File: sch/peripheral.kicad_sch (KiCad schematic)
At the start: 0 parts

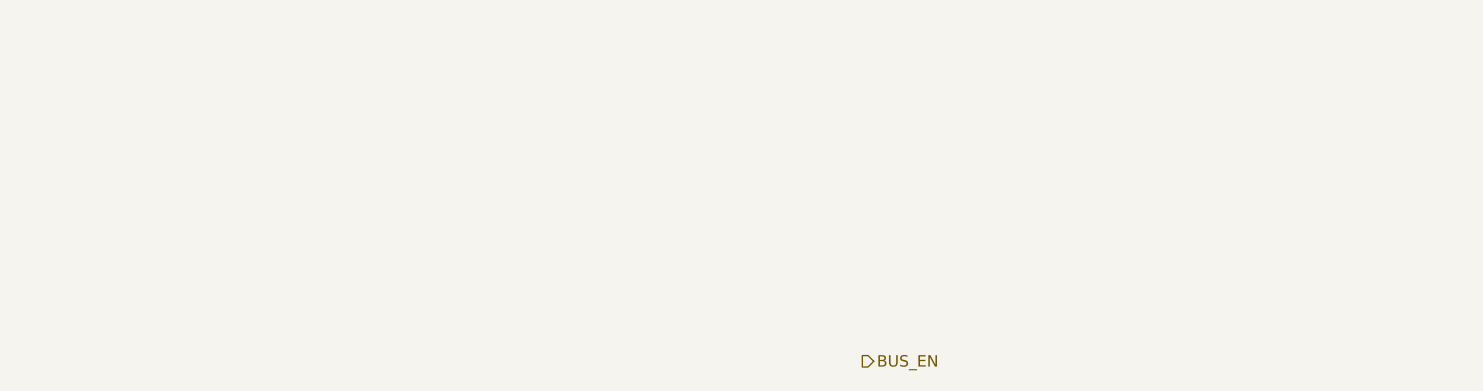
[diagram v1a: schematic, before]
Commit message: Board layout, addr bus
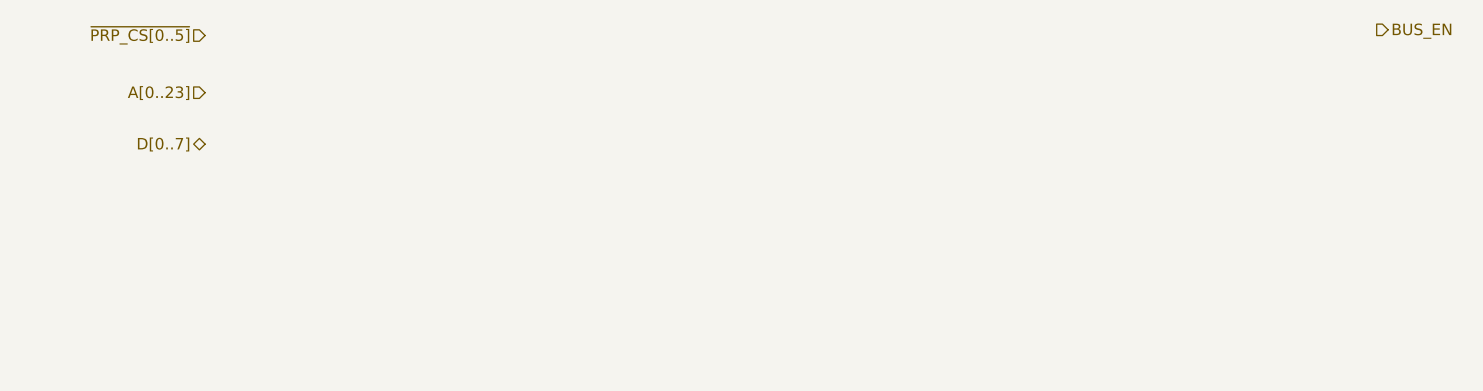
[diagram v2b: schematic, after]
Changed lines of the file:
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@@
 (kicad_sch (version 20211123) (generator eeschema)
   (paper "A4")
-  (hierarchical_label "BUS_EN" (shape output) (at 149.86 100.33 0)
+  (hierarchical_label "BUS_EN" (shape output) (at 207.01 63.5 0)
     (effects (font (size 1.27 1.27)) (justify left))
   )
+  (hierarchical_label "A[0..23]" (shape input) (at 76.835 70.485 180)
+    (effects (font (size 1.27 1.27)) (justify right))
+  )
+  (hierarchical_label "~{PRP_CS[0..5]}" (shape input) (at 76.835 64.135 180)
+    (effects (font (size 1.27 1.27)) (justify right))
+  )
+  (hierarchical_label "D[0..7]" (shape bidirectional) (at 76.835 76.2 180)
+    (effects (font (size 1.27 1.27)) (justify right))
+  )
 )

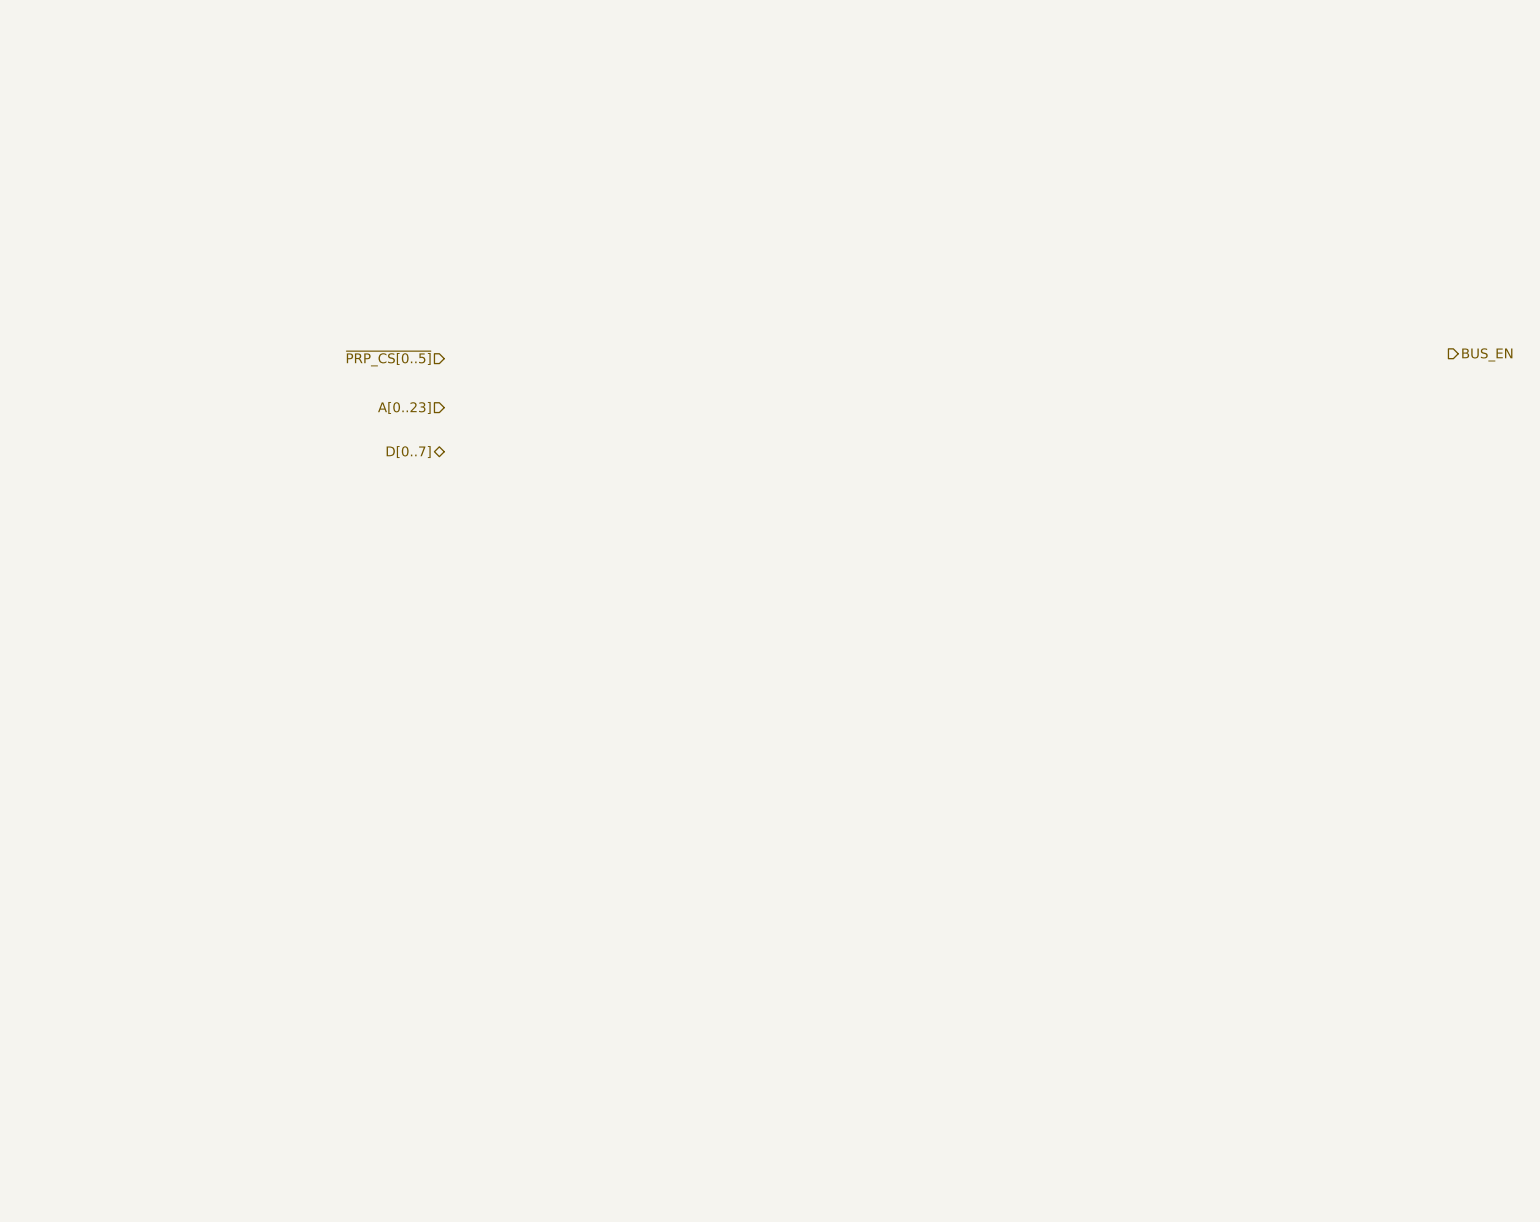
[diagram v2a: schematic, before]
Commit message: More routing, USB iface
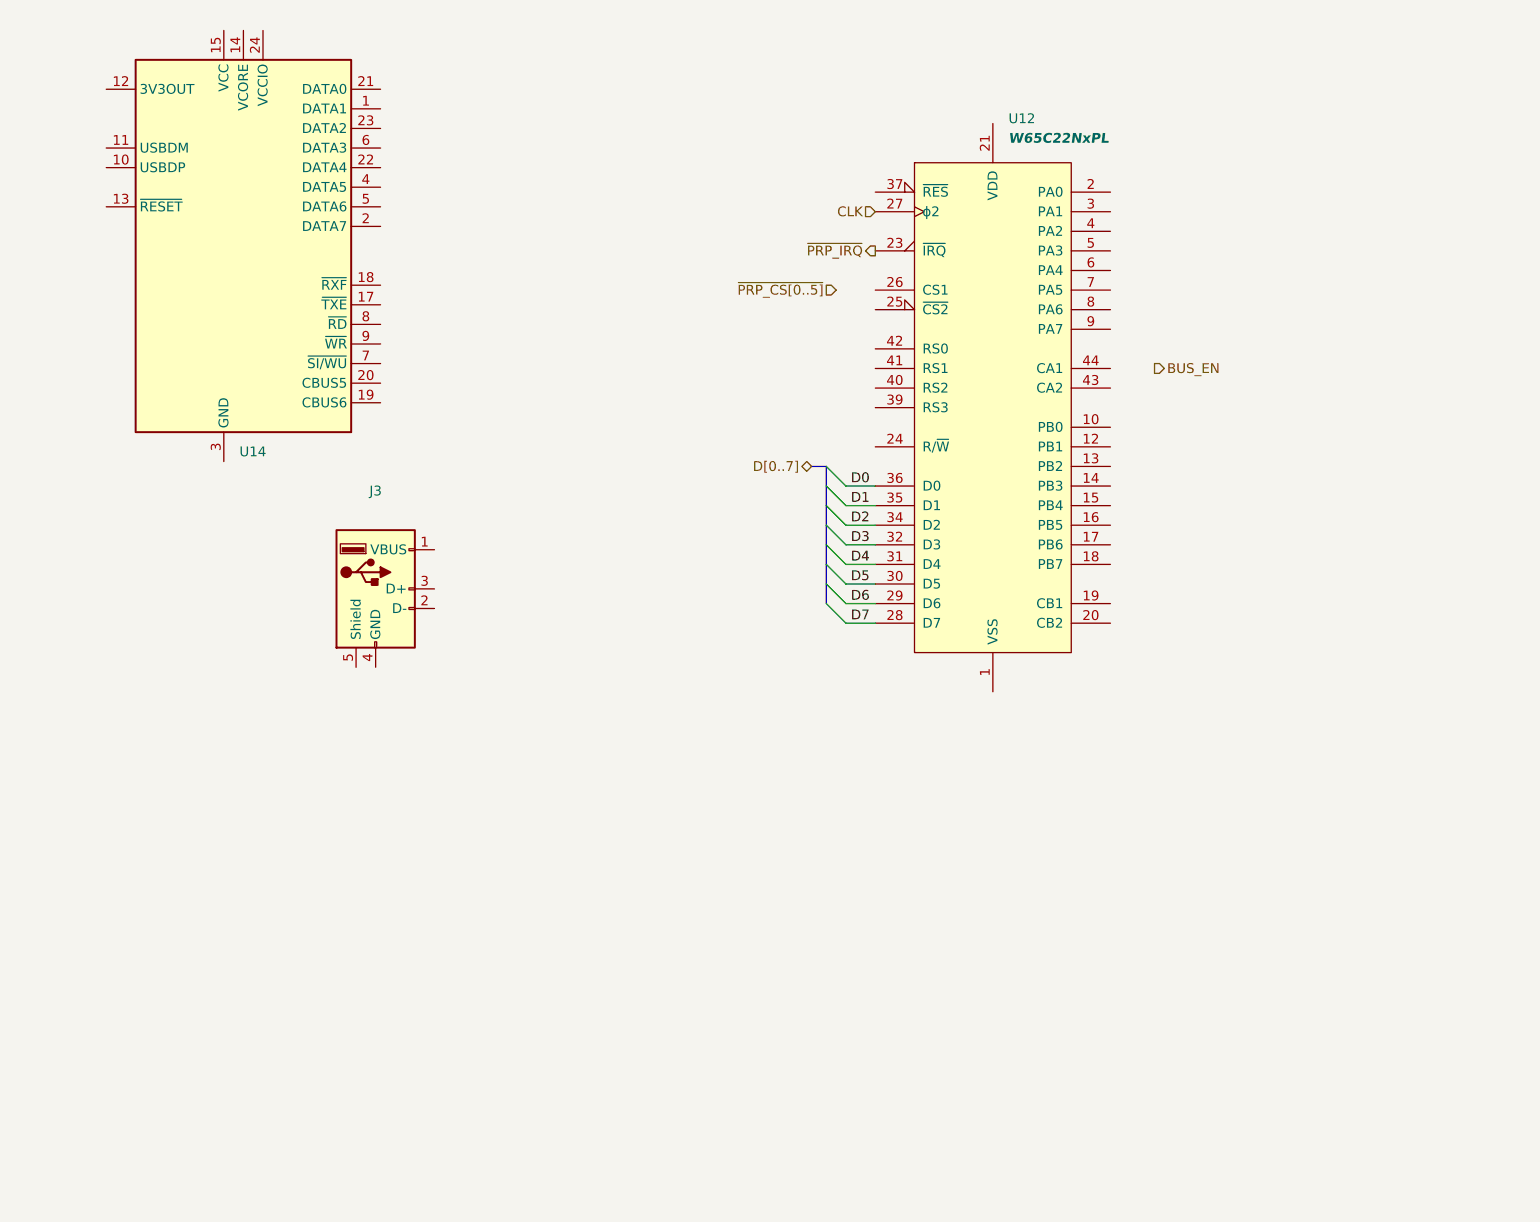
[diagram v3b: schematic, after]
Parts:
- added J3: (no value), symbol Connector:USB_A
- added U12: W65C22NxPL, symbol 65xx:W65C22NxPL
- added U14: (no value), symbol Interface_USB:FT240XQ
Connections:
- new net: U14.16 (GND), U14.25 (GND), U14.3 (GND)
- new net CLK: U12.27 (ϕ2)
- new net D0: U12.36 (D0)
- new net D1: U12.35 (D1)
- new net D2: U12.34 (D2)
- new net D3: U12.32 (D3)
- new net D4: U12.31 (D4)
- new net D5: U12.30 (D5)
- new net D6: U12.29 (D6)
- new net D7: U12.28 (D7)
- new net ~{PRP_IRQ}: U12.23 (~{IRQ})
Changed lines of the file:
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@@
 (kicad_sch (version 20211123) (generator eeschema)
   (paper "A4")
-  (hierarchical_label "BUS_EN" (shape output) (at 207.01 63.5 0)
+  (bus_entry (at 126.365 78.105) (size 2.54 2.54)
+    (stroke (width 0) (type default) (color 0 0 0 0))
+  )
+  (bus_entry (at 126.365 93.345) (size 2.54 2.54)
+    (stroke (width 0) (type default) (color 0 0 0 0))
+  )
+  (bus_entry (at 126.365 90.805) (size 2.54 2.54)
+    (stroke (width 0) (type default) (color 0 0 0 0))
+  )
+  (bus_entry (at 126.365 85.725) (size 2.54 2.54)
+    (stroke (width 0) (type default) (color 0 0 0 0))
+  )
+  (bus_entry (at 126.365 88.265) (size 2.54 2.54)
+    (stroke (width 0) (type default) (color 0 0 0 0))
+  )
+  (bus_entry (at 126.365 83.185) (size 2.54 2.54)
+    (stroke (width 0) (type default) (color 0 0 0 0))
+  )
+  (bus_entry (at 126.365 80.645) (size 2.54 2.54)
+    (stroke (width 0) (type default) (color 0 0 0 0))
+  )
+  (bus_entry (at 126.365 95.885) (size 2.54 2.54)
+    (stroke (width 0) (type default) (color 0 0 0 0))
+  )
+  (bus (pts (xy 126.365 93.345) (xy 126.365 95.885))
+    (stroke (width 0) (type default) (color 0 0 0 0))
+  )
+  (bus (pts (xy 126.365 83.185) (xy 126.365 85.725))
+    (stroke (width 0) (type default) (color 0 0 0 0))
+  )
+  (wire (pts (xy 128.905 83.185) (xy 132.715 83.185))
+    (stroke (width 0) (type default) (color 0 0 0 0))
+  )
+  (wire (pts (xy 128.905 90.805) (xy 132.715 90.805))
+    (stroke (width 0) (type default) (color 0 0 0 0))
+  )
+  (wire (pts (xy 128.905 98.425) (xy 132.715 98.425))
+    (stroke (width 0) (type default) (color 0 0 0 0))
+  )
+  (bus (pts (xy 126.365 80.645) (xy 126.365 83.185))
+    (stroke (width 0) (type default) (color 0 0 0 0))
+  )
+  (bus (pts (xy 126.365 88.265) (xy 126.365 90.805))
+    (stroke (width 0) (type default) (color 0 0 0 0))
+  )
+  (wire (pts (xy 128.905 80.645) (xy 132.715 80.645))
+    (stroke (width 0) (type default) (color 0 0 0 0))
+  )
+  (wire (pts (xy 128.905 85.725) (xy 132.715 85.725))
+    (stroke (width 0) (type default) (color 0 0 0 0))
+  )
+  (wire (pts (xy 128.905 95.885) (xy 132.715 95.885))
+    (stroke (width 0) (type default) (color 0 0 0 0))
+  )
+  (bus (pts (xy 124.46 78.105) (xy 126.365 78.105))
+    (stroke (width 0) (type default) (color 0 0 0 0))
+  )
+  (wire (pts (xy 128.905 88.265) (xy 132.715 88.265))
+    (stroke (width 0) (type default) (color 0 0 0 0))
+  )
+  (bus (pts (xy 126.365 85.725) (xy 126.365 88.265))
+    (stroke (width 0) (type default) (color 0 0 0 0))
+  )
+  (bus (pts (xy 126.365 90.805) (xy 126.365 93.345))
+    (stroke (width 0) (type default) (color 0 0 0 0))
+  )
+  (bus (pts (xy 126.365 78.105) (xy 126.365 80.645))
+    (stroke (width 0) (type default) (color 0 0 0 0))
+  )
+  (wire (pts (xy 128.905 93.345) (xy 132.715 93.345))
+    (stroke (width 0) (type default) (color 0 0 0 0))
+  )
+  (label "D2" (at 129.54 85.725 0)
+    (effects (font (size 1.27 1.27)) (justify left bottom))
+  )
+  (label "D7" (at 129.54 98.425 0)
+    (effects (font (size 1.27 1.27)) (justify left bottom))
+  )
+  (label "D1" (at 129.54 83.185 0)
+    (effects (font (size 1.27 1.27)) (justify left bottom))
+  )
+  (label "D4" (at 129.54 90.805 0)
+    (effects (font (size 1.27 1.27)) (justify left bottom))
+  )
+  (label "D6" (at 129.54 95.885 0)
+    (effects (font (size 1.27 1.27)) (justify left bottom))
+  )
+  (label "D3" (at 129.54 88.265 0)
+    (effects (font (size 1.27 1.27)) (justify left bottom))
+  )
+  (label "D0" (at 129.54 80.645 0)
+    (effects (font (size 1.27 1.27)) (justify left bottom))
+  )
+  (label "D5" (at 129.54 93.345 0)
+    (effects (font (size 1.27 1.27)) (justify left bottom))
+  )
+  (hierarchical_label "~{PRP_IRQ}" (shape output) (at 132.715 50.165 180)
+    (effects (font (size 1.27 1.27)) (justify right))
+  )
+  (hierarchical_label "CLK" (shape input) (at 132.715 45.085 180)
+    (effects (font (size 1.27 1.27)) (justify right))
+  )
+  (hierarchical_label "BUS_EN" (shape output) (at 168.91 65.405 0)
     (effects (font (size 1.27 1.27)) (justify left))
   )
-  (hierarchical_label "A[0..23]" (shape input) (at 76.835 70.485 180)
-    (effects (font (size 1.27 1.27)) (justify right))
-  )
-  (hierarchical_label "~{PRP_CS[0..5]}" (shape input) (at 76.835 64.135 180)
-    (effects (font (size 1.27 1.27)) (justify right))
-  )
-  (hierarchical_label "D[0..7]" (shape bidirectional) (at 76.835 76.2 180)
-    (effects (font (size 1.27 1.27)) (justify right))
+  (hierarchical_label "~{PRP_CS[0..5]}" (shape input) (at 127.635 55.245 180)
+    (effects (font (size 1.27 1.27)) (justify right))
+  )
+  (hierarchical_label "D[0..7]" (shape bidirectional) (at 124.46 78.105 180)
+    (effects (font (size 1.27 1.27)) (justify right))
+  )
+  (symbol (lib_id "Interface_USB:FT240XQ") (at 50.8 49.53 0) (unit 1)
+    (in_bom yes) (on_board yes) (fields_autoplaced)
+    (property "Reference" "U14" (id 0) (at 50.2794 76.2 0)
+      (effects (font (size 1.27 1.27)) (justify left))
+    )
+    (property "Value" "" (id 1) (at 50.2794 78.74 0)
+      (effects (font (size 1.27 1.27)) (justify left))
+    )
+    (property "Footprint" "" (id 2) (at 85.09 74.93 0)
+      (effects (font (size 1.27 1.27)) hide)
+    )
+    (property "Datasheet" "https://www.ftdichip.com/Support/Documents/DataSheets/ICs/DS_FT240X.pdf" (id 3) (at 50.8 49.53 0)
+      (effects (font (size 1.27 1.27)) hide)
+    )
+    (pin "1")
+    (pin "10")
+    (pin "11")
+    (pin "12")
+    (pin "13")
+    (pin "14")
+    (pin "15")
+    (pin "16")
+    (pin "17")
+    (pin "18")
+    (pin "19")
+    (pin "2")
+    (pin "20")
+    (pin "21")
+    (pin "22")
+    (pin "23")
+    (pin "24")
+    (pin "25")
+    (pin "3")
+    (pin "4")
+    (pin "5")
+    (pin "6")
+    (pin "7")
+    (pin "8")
+    (pin "9")
+  )
+  (symbol (lib_id "Connector:USB_A") (at 67.945 93.98 0) (unit 1)
+    (in_bom yes) (on_board yes) (fields_autoplaced)
+    (property "Reference" "J3" (id 0) (at 67.945 81.28 0))
+    (property "Value" "" (id 1) (at 67.945 83.82 0))
+    (property "Footprint" "" (id 2) (at 71.755 95.25 0)
+      (effects (font (size 1.27 1.27)) hide)
+    )
+    (property "Datasheet" " ~" (id 3) (at 71.755 95.25 0)
+      (effects (font (size 1.27 1.27)) hide)
+    )
+    (pin "1")
+    (pin "2")
+    (pin "3")
+    (pin "4")
+    (pin "5")
+  )
+  (symbol (lib_id "65xx:W65C22NxPL") (at 147.955 70.485 0) (unit 1)
+    (in_bom yes) (on_board yes) (fields_autoplaced)
+    (property "Reference" "U12" (id 0) (at 149.9744 33.02 0)
+      (effects (font (size 1.27 1.27)) (justify left))
+    )
+    (property "Value" "W65C22NxPL" (id 1) (at 149.9744 35.56 0)
+      (effects (font (size 1.27 1.27) bold italic) (justify left))
+    )
+    (property "Footprint" "" (id 2) (at 147.955 66.675 0)
+      (effects (font (size 1.27 1.27)) hide)
+    )
+    (property "Datasheet" "http://www.westerndesigncenter.com/wdc/documentation/w65c22.pdf" (id 3) (at 147.955 66.675 0)
+      (effects (font (size 1.27 1.27)) hide)
+    )
+    (pin "1")
+    (pin "10")
+    (pin "11")
+    (pin "12")
+    (pin "13")
+    (pin "14")
+    (pin "15")
+    (pin "16")
+    (pin "17")
+    (pin "18")
+    (pin "19")
+    (pin "2")
+    (pin "20")
+    (pin "21")
+    (pin "22")
+    (pin "23")
+    (pin "24")
+    (pin "25")
+    (pin "26")
+    (pin "27")
+    (pin "28")
+    (pin "29")
+    (pin "3")
+    (pin "30")
+    (pin "31")
+    (pin "32")
+    (pin "33")
+    (pin "34")
+    (pin "35")
+    (pin "36")
+    (pin "37")
+    (pin "38")
+    (pin "39")
+    (pin "4")
+    (pin "40")
+    (pin "41")
+    (pin "42")
+    (pin "43")
+    (pin "44")
+    (pin "5")
+    (pin "6")
+    (pin "7")
+    (pin "8")
+    (pin "9")
   )
 )

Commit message: Pivot to 6502
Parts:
- J3: value (none) -> USB_A; footprint (none) -> Connector_USB:USB_A_TE_292303-7_Horizontal
- U12: footprint (none) -> Package_QFP:PQFP-44_10x10mm_P0.8mm
- U14: value (none) -> FT240XQ; footprint (none) -> Package_DFN_QFN:QFN-24-1EP_4x4mm_P0.5mm_EP2.6x2.6mm
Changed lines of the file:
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@@
       (effects (font (size 1.27 1.27)) (justify left))
     )
-    (property "Value" "" (id 1) (at 50.2794 78.74 0)
+    (property "Value" "FT240XQ" (id 1) (at 50.2794 78.74 0)
       (effects (font (size 1.27 1.27)) (justify left))
     )
-    (property "Footprint" "" (id 2) (at 85.09 74.93 0)
+    (property "Footprint" "Package_DFN_QFN:QFN-24-1EP_4x4mm_P0.5mm_EP2.6x2.6mm" (id 2) (at 85.09 74.93 0)
       (effects (font (size 1.27 1.27)) hide)
     )
@@
     (in_bom yes) (on_board yes) (fields_autoplaced)
     (property "Reference" "J3" (id 0) (at 67.945 81.28 0))
-    (property "Value" "" (id 1) (at 67.945 83.82 0))
-    (property "Footprint" "" (id 2) (at 71.755 95.25 0)
+    (property "Value" "USB_A" (id 1) (at 67.945 83.82 0))
+    (property "Footprint" "Connector_USB:USB_A_TE_292303-7_Horizontal" (id 2) (at 71.755 95.25 0)
       (effects (font (size 1.27 1.27)) hide)
     )
@@
       (effects (font (size 1.27 1.27) bold italic) (justify left))
     )
-    (property "Footprint" "" (id 2) (at 147.955 66.675 0)
+    (property "Footprint" "Package_QFP:PQFP-44_10x10mm_P0.8mm" (id 2) (at 147.955 66.675 0)
       (effects (font (size 1.27 1.27)) hide)
     )

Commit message: Serial interface
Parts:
- removed U12: W65C22NxPL, Package_QFP:PQFP-44_10x10mm_P0.8mm, symbol 65xx:W65C22NxPL
- added PRP1: W65C22SxQ, Package_QFP:PQFP-44_10x10mm_P0.8mm, symbol 65xx:W65C22SxQ
- renumbered U14 to USB1
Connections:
- net CLK: now also PRP1.21 (ϕ2)
- net D0: now also PRP1.30 (D0)
- net D1: now also PRP1.29 (D1)
- net D2: now also PRP1.28 (D2)
- net D3: now also PRP1.26 (D3)
- net D4: now also PRP1.25 (D4)
- net D5: now also PRP1.24 (D5)
- net D6: now also PRP1.23 (D6)
- net D7: now also PRP1.22 (D7)
- net ~{PRP_IRQ}: now also PRP1.17 (~{IRQ})
- net PD1: now reaches USB1.1 (DATA1)
- net PD1: now also PRP1.6 (PB1)
- net at USB1.10 (USBDP): now also J3.3 (D+)
- net at USB1.11 (USBDM): now also J3.2 (D-)
- net at USB1.12 (3V3OUT): now also USB1.24 (VCCIO)
- net ~{RESET}: now reaches USB1.13 (~{RESET})
- net ~{RESET}: now also PRP1.31 (~{RES})
- net +5V: now reaches USB1.15 (VCC)
- net +5V: now also PRP1.15 (VDD)
- net GND: now reaches USB1.16 (GND), USB1.25 (GND), USB1.3 (GND)
- net GND: now also J3.4 (GND), J3.5 (Shield), PRP1.39 (VSS)
- net PD7: now reaches USB1.2 (DATA7)
- net PD7: now also PRP1.12 (PB7)
- net PD0: now reaches USB1.21 (DATA0)
- net PD0: now also PRP1.4 (PB0)
- net PD4: now reaches USB1.22 (DATA4)
- net PD4: now also PRP1.9 (PB4)
- net PD2: now reaches USB1.23 (DATA2)
- net PD2: now also PRP1.7 (PB2)
- net PD5: now reaches USB1.4 (DATA5)
- net PD5: now also PRP1.10 (PB5)
- net PD6: now reaches USB1.5 (DATA6)
- net PD6: now also PRP1.11 (PB6)
- net PD3: now reaches USB1.6 (DATA3)
- net PD3: now also PRP1.8 (PB3)
- new net A0: PRP1.36 (RS0)
- new net A1: PRP1.35 (RS1)
- new net A15: PRP1.20 (CS1)
- new net A2: PRP1.34 (RS2)
- new net A3: PRP1.33 (RS3)
- new net BUS_R~{W}: PRP1.18 (R/~{W})
- new net ~{PRP_CS}: PRP1.19 (~{CS2})
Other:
- company: (none) -> zrthxn
- title: (none) -> 8puter
- moved on the sheet: J3, USB1
